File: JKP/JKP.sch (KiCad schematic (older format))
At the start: 225 parts, among them J1 Conn_01x04_Male, SW1 SW_Push, U1 ATmega32U4-AU, Y1 16MHz

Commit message: physical pcb components placement 40% done
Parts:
- MX80: footprint MX_Alps_Hybrid:MX-1U-NoLED -> MX_Alps_Hybrid:MX-2U-ReversedStabilizers-NoLED
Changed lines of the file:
@@
 F 0 "MX80" H 13833 4823 60  0000 C CNN
 F 1 "Num0" H 13833 4749 20  0000 C CNN
-F 2 "MX_Alps_Hybrid:MX-1U-NoLED" H 13175 4575 60  0001 C CNN
+F 2 "MX_Alps_Hybrid:MX-2U-ReversedStabilizers-NoLED" H 13175 4575 60  0001 C CNN
 F 3 "" H 13175 4575 60  0001 C CNN
 	1    13800 4600

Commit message: routing pcb part 1
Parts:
- added MX97: MX-NoLED, MX_Alps_Hybrid:MX-1.5U-NoLED, symbol MX_Alps_Hybrid:MX-NoLED
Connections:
- net +5V: now also D1.1 (VDD), D14.1 (VDD), D2.1 (VDD), D27.1 (VDD), D3.1 (VDD), D33.1 (VDD), D39.1 (VDD), D4.1 (VDD), D45.1 (VDD), D5.1 (VDD), D52.1 (VDD), D58.1 (VDD), D6.1 (VDD), D64.1 (VDD), D7.1 (VDD), D70.1 (VDD)
- net COL0: now also MX97.1 (COL)
- net COL10: now also MX50.1 (COL); no longer MX55.1 (COL)
- net COL11: now also MX55.1 (COL); no longer MX61.1 (COL)
- net COL12: now also MX61.1 (COL); no longer MX67.1 (COL)
- net COL13: now also MX67.1 (COL)
- net COL14: no longer MX80.1 (COL)
- net COL15: now also MX80.1 (COL)
- net COL5: no longer MX29.1 (COL)
- net COL6: now also MX29.1 (COL); no longer MX34.1 (COL)
- net COL7: now also MX34.1 (COL); no longer MX40.1 (COL)
- net COL8: now also MX40.1 (COL); no longer MX45.1 (COL)
- net COL9: now also MX45.1 (COL); no longer MX50.1 (COL)
- net GND: now also D1.3 (VSS), D14.3 (VSS), D2.3 (VSS), D27.3 (VSS), D3.3 (VSS), D33.3 (VSS), D39.3 (VSS), D4.3 (VSS), D45.3 (VSS), D5.3 (VSS), D52.3 (VSS), D58.3 (VSS), D6.3 (VSS), D64.3 (VSS), D7.3 (VSS), D70.3 (VSS)
- net ROW4: no longer D112.1 (K)
- net ROW5: now also D112.1 (K)
- net at D11.2 (A), MX4.2 (ROW): now also MX97.2 (ROW)
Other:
- moved on the sheet: D112, D40, D46, D53, D59, D65, D71, D77, D83, D96, MX29, MX34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

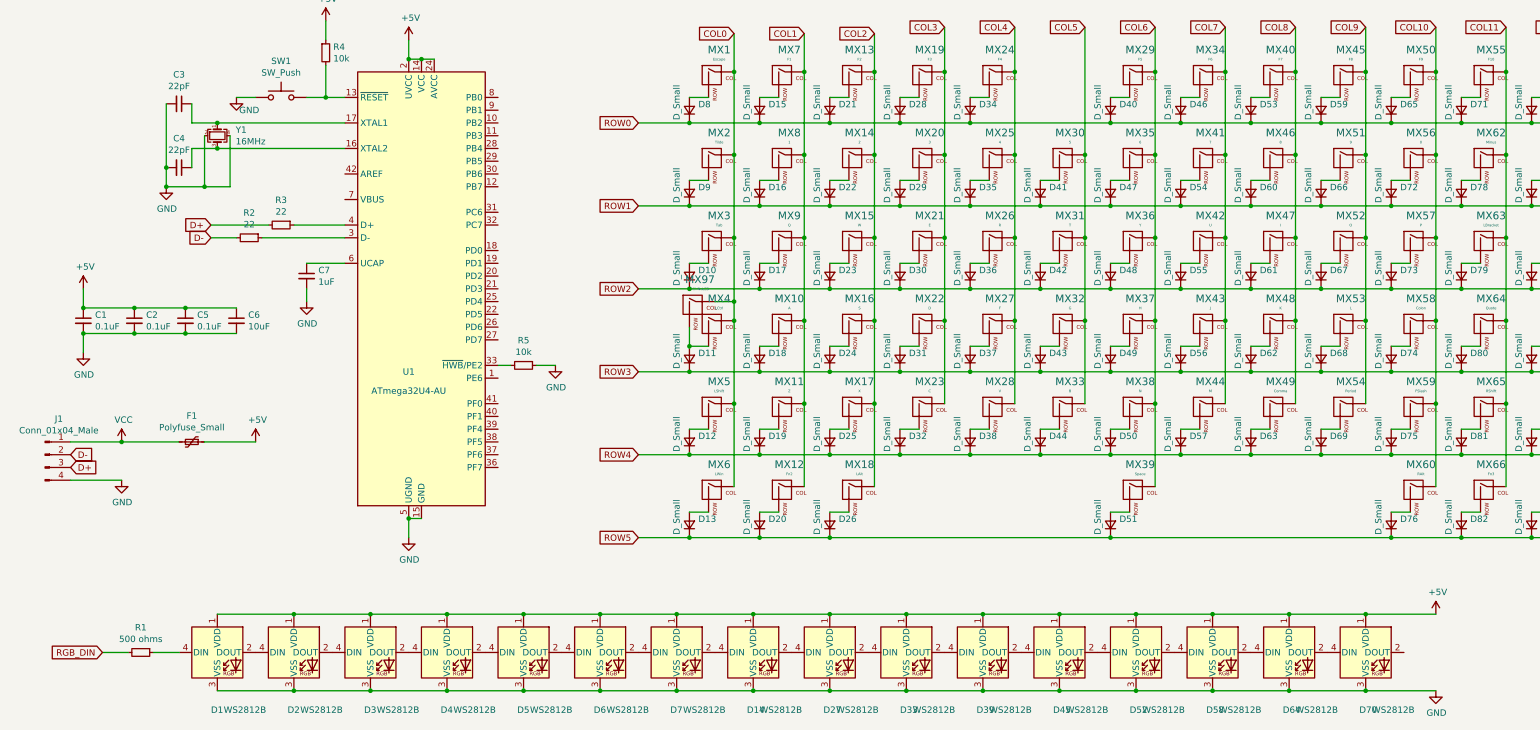
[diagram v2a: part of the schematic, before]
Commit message: Finished PCB v1 No LED
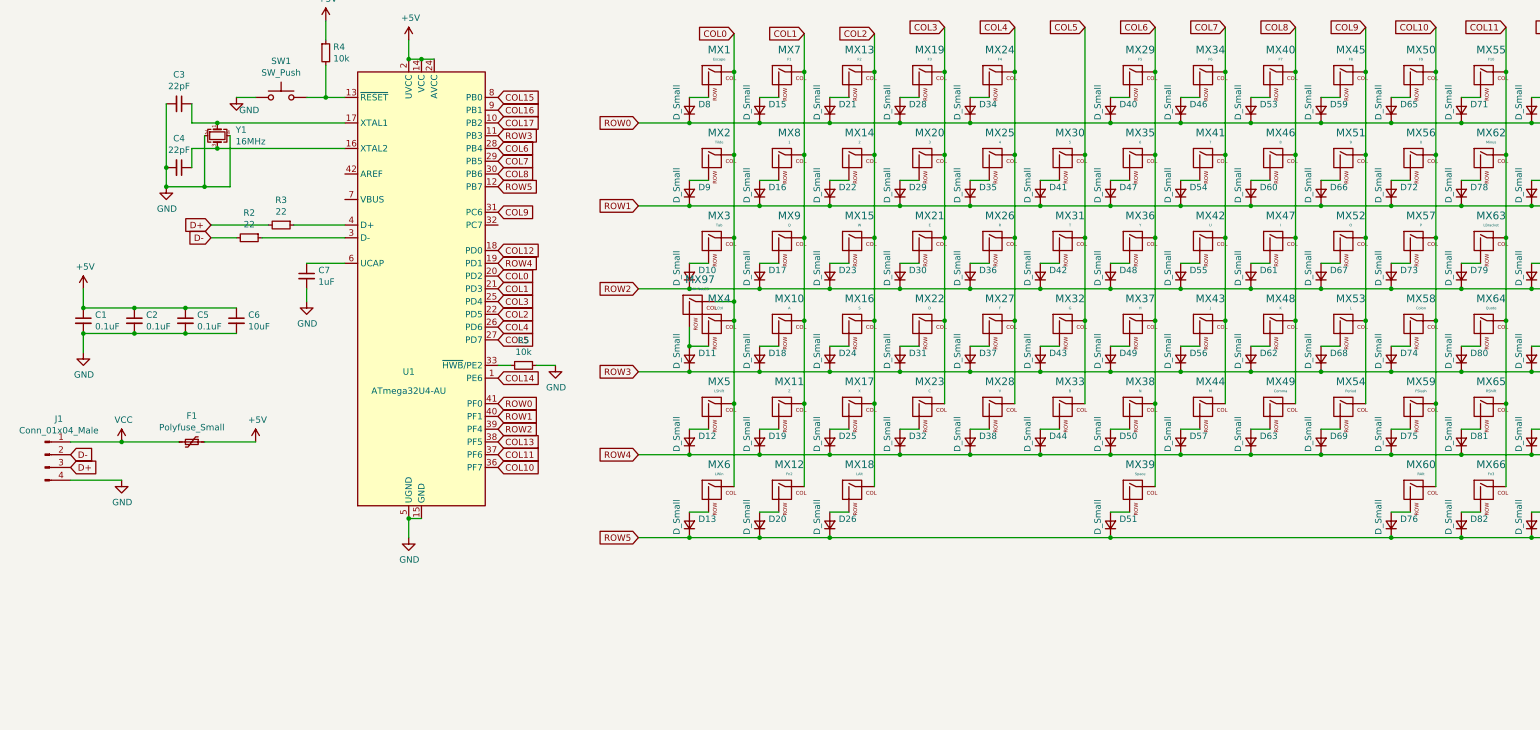
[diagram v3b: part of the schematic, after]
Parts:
- removed D1, D14, D2, D27, D3, D33, D39, D4, D45, D5, D52, D58, D6, D64, D7, D70: WS2812B, LED_SMD:LED_WS2812B_PLCC4_5.0x5.0mm_P3.2mm, symbol LED:WS2812B
- removed R1: 500 ohms, Resistor_SMD:R_0805_2012Metric, symbol Device:R_Small
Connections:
- net COL0: now also U1.20 (PD2)
- net COL1: now also U1.21 (PD3)
- net COL10: now also U1.36 (PF7)
- net COL11: now also U1.37 (PF6)
- net COL12: now also U1.18 (PD0)
- net COL13: now also U1.38 (PF5)
- net COL14: now also U1.1 (PE6)
- net COL15: now also U1.8 (PB0)
- net COL16: now also U1.9 (PB1)
- net COL17: now also U1.10 (PB2)
- net COL2: now also U1.22 (PD5)
- net COL3: now also U1.25 (PD4)
- net COL4: now also U1.26 (PD6)
- net COL5: now also U1.27 (PD7)
- net COL6: now also U1.28 (PB4)
- net COL7: now also U1.29 (PB5)
- net COL8: now also U1.30 (PB6)
- net COL9: now also U1.31 (PC6)
- net ROW0: now also U1.41 (PF0)
- net ROW1: now also U1.40 (PF1)
- net ROW2: now also U1.39 (PF4)
- net ROW3: now also U1.11 (PB3)
- net ROW4: now also U1.19 (PD1)
- net ROW5: now also U1.12 (PB7)

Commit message: final PCB v1
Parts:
- renumbered D8 to D1, D18 to D10, D19 to D11, D20 to D12, D21 to D13, D22 to D14, D23 to D15, D24 to D16, D25 to D17, D26 to D18, D28 to D19, D9 to D2, D29 to D20, D30 to D21, D31 to D22, D32 to D23, D34 to D24, D35 to D25, D36 to D26, D37 to D27, D38 to D28, D41 to D29, D10 to D3, D42 to D30, D43 to D31, D44 to D32, D40 to D33, D47 to D34, D48 to D35, D49 to D36, D50 to D37, D51 to D38, D46 to D39, D11 to D4, D54 to D40, D55 to D41, D56 to D42, D57 to D43, D53 to D44, D60 to D45, D61 to D46, D62 to D47, D63 to D48, D59 to D49, D12 to D5, D66 to D50, D67 to D51, D68 to D52, D69 to D53, D65 to D54, D72 to D55, D73 to D56, D74 to D57, D75 to D58, D76 to D59, D13 to D6, D71 to D60, D78 to D61, D79 to D62, D80 to D63, D81 to D64, D82 to D65, D77 to D66, D84 to D67, D85 to D68, D86 to D69, D15 to D7, D87 to D70, D88 to D71, D83 to D72, D89 to D73, D90 to D74, D91 to D75, D92 to D76, D93 to D77, D94 to D78, D95 to D79, D16 to D8, D97 to D80, D98 to D81, D99 to D82, D100 to D83, D101 to D84, D96 to D85, D102 to D86, D103 to D87, D104 to D88, D105 to D89, D17 to D9, D106 to D90, D107 to D91, D108 to D92, D109 to D93, D110 to D94, D111 to D95, D112 to D96, MX97 to MX1, MX9 to MX10, MX10 to MX11, MX11 to MX12, MX12 to MX13, MX13 to MX14, MX14 to MX15, MX15 to MX16, MX16 to MX17, MX17 to MX18, MX18 to MX19, MX1 to MX2, MX19 to MX20, MX20 to MX21, MX21 to MX22, MX22 to MX23, MX23 to MX24, MX24 to MX25, MX25 to MX26, MX26 to MX27, MX27 to MX28, MX28 to MX29, MX2 to MX3, MX29 to MX34, MX3 to MX4, MX34 to MX40, MX40 to MX45, MX4 to MX5, MX45 to MX50, MX50 to MX55, MX5 to MX6, MX55 to MX61, MX61 to MX67, MX6 to MX7, MX67 to MX73, MX73 to MX74, MX74 to MX75, MX75 to MX76, MX76 to MX77, MX77 to MX78, MX78 to MX79, MX7 to MX8, MX79 to MX80, MX80 to MX86, MX86 to MX87, MX87 to MX88, MX88 to MX89, MX8 to MX9, MX89 to MX90, MX90 to MX91, MX91 to MX92, MX92 to MX93, MX93 to MX94, MX94 to MX95, MX95 to MX96, MX96 to MX97, R2 to R1, R3 to R2, R4 to R3, R5 to R4

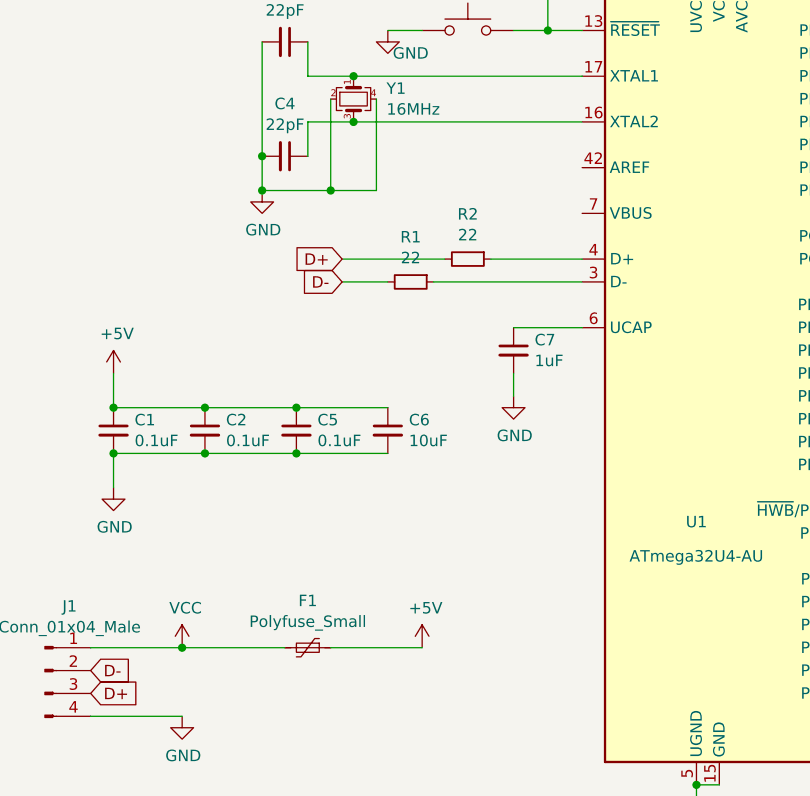
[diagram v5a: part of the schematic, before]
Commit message: fixed VBUS not connected
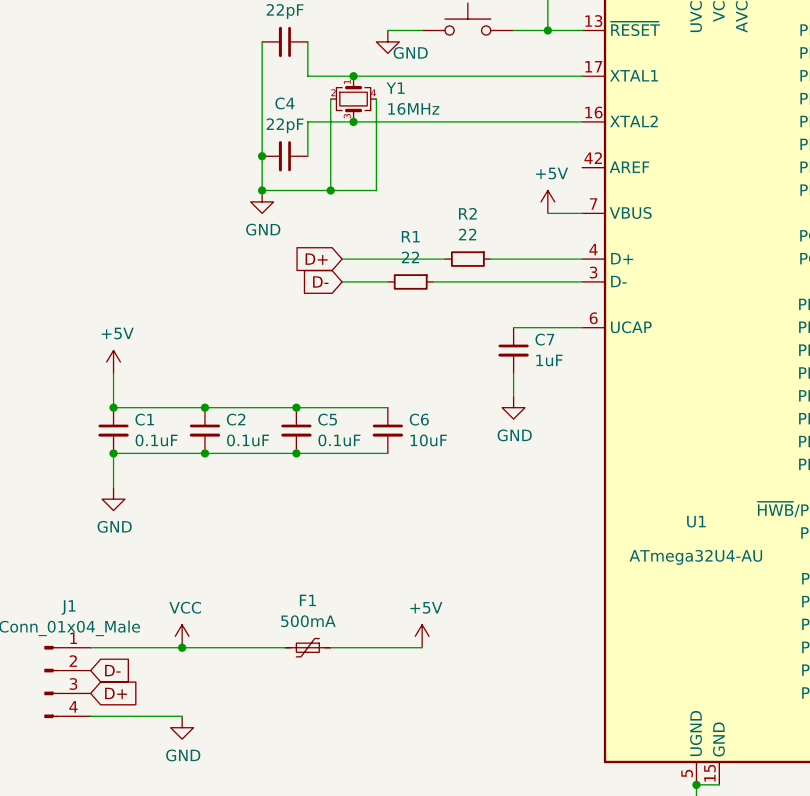
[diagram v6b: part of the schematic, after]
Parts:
- F1: value Polyfuse_Small -> 500mA
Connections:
- net +5V: now also U1.7 (VBUS)
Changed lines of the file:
@@
 P 2000 4200
 F 0 "F1" V 1795 4200 50  0000 C CNN
-F 1 "Polyfuse_Small" V 1886 4200 50  0000 C CNN
+F 1 "500mA" V 1886 4200 50  0000 C CNN
 F 2 "Fuse:Fuse_1206_3216Metric" H 2050 4000 50  0001 L CNN
 F 3 "~" H 2000 4200 50  0001 C CNN
@@
 	1    0    0    -1
 $EndComp
+$Comp
+L power:+5V #PWR0101
+U 1 1 61D3363A
+P 3050 2300
+F 0 "#PWR0101" H 3050 2150 50  0001 C CNN
+F 1 "+5V" H 3065 2473 50  0000 C CNN
+F 2 "" H 3050 2300 50  0001 C CNN
+F 3 "" H 3050 2300 50  0001 C CNN
+	1    3050 2300
+	1    0    0    -1
+$EndComp
+Wire Wire Line
+	3200 2300 3050 2300
 $EndSCHEMATC
